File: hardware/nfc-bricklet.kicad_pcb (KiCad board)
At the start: 2 copper layers, 85 x 50 mm, 53 parts, among them J1 CONN_01X03, P1 CON-SENSOR2, U1 XMC130024, U2 PN7150, U3 DRILL, U4 DRILL, U5 DRILL, U6 DRILL, U7 DRILL, U8 DRILL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

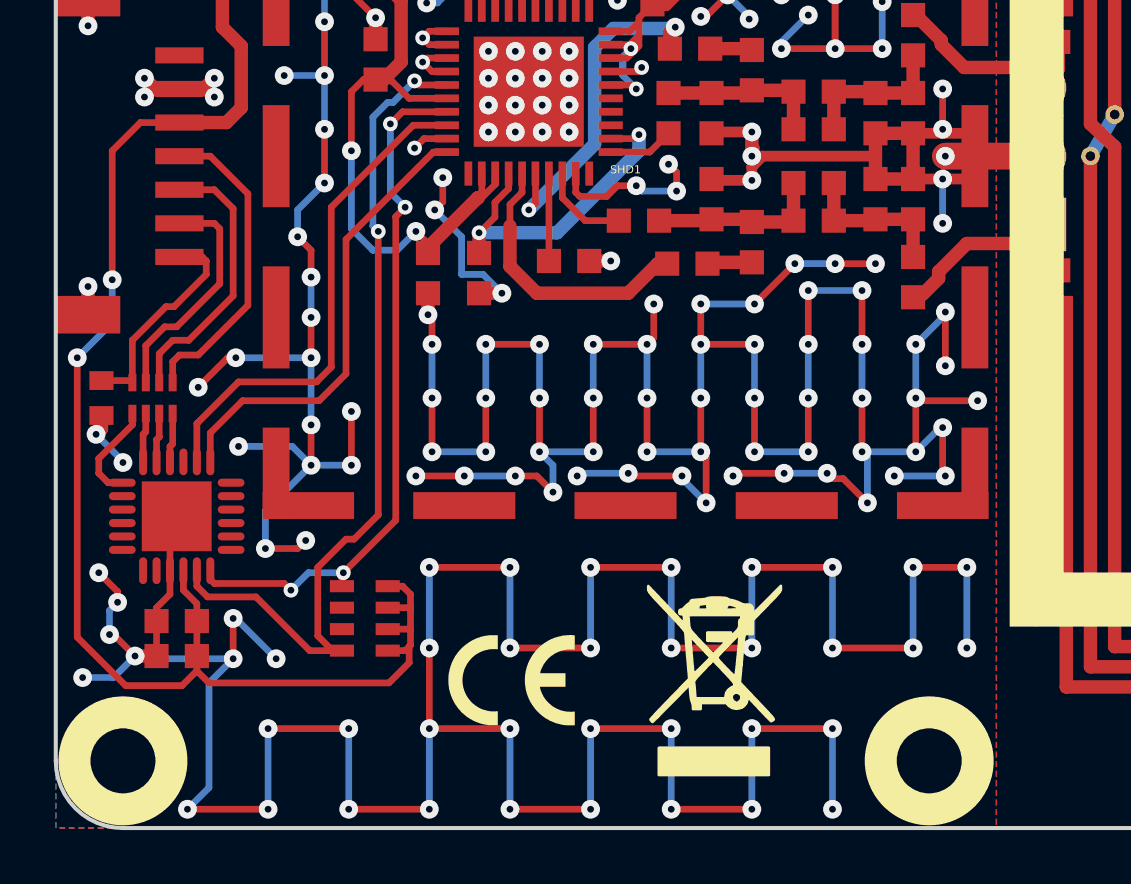
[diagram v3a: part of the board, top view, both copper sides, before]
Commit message: add status led, debug pad, boot pad
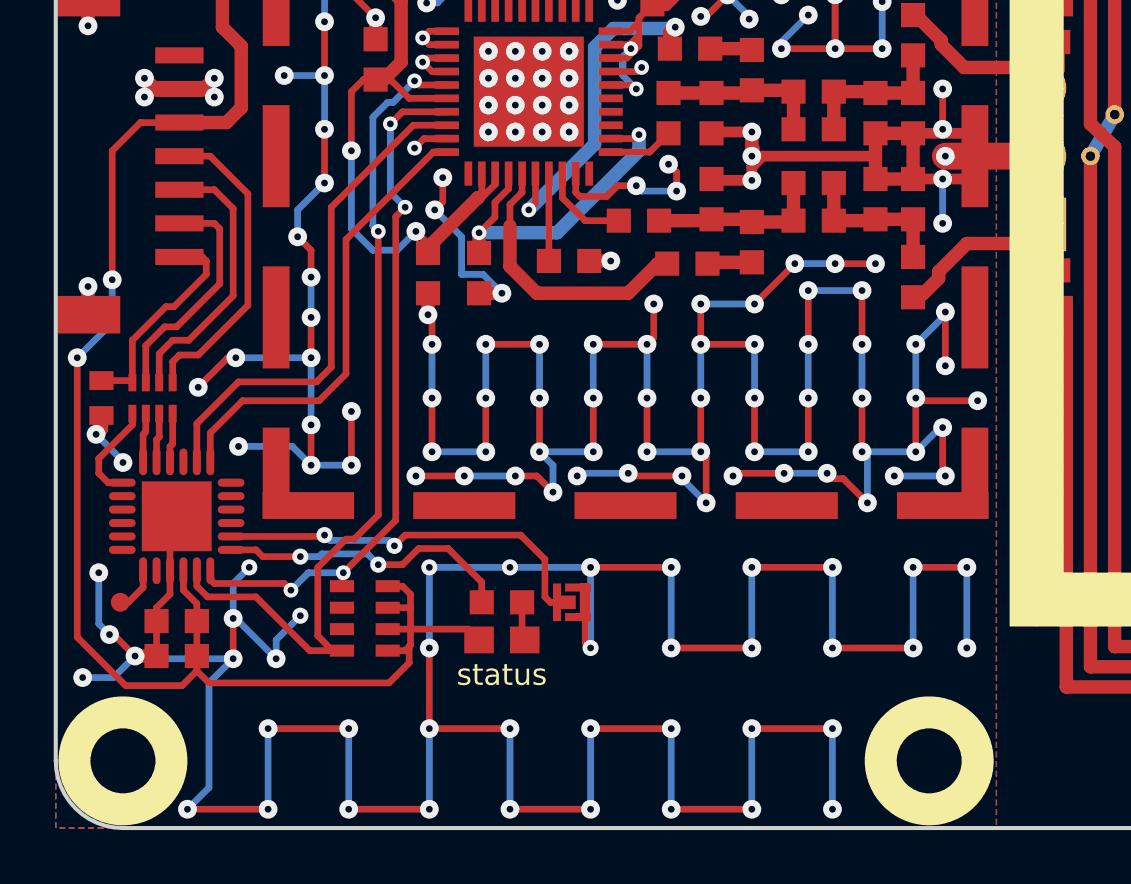
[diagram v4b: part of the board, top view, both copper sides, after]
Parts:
- added D1: blue, D0603E, F.Cu at (127.0, 95.0)
- added P2: BOOT, kicad-libraries:SolderJumper, F.Cu at (129.6, 93.6)
- added P3: DEBUG, kicad-libraries:DEBUG_PAD, F.Cu at (112.8, 93.6)
- added R7: 1k, R0603F, F.Cu at (127.0, 93.6)
- VAL (x2): moved to B.Cu
- moved VAL 20.9 mm to (127.4, 77.0)
- moved VAL 20.7 mm to (120.4, 77.0)
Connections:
- U1 pad 13: (no net) -> Net-(R7-Pad1)
- U1 pad 14: (no net) -> Net-(P2-Pad2)
- U1 pad 7: (no net) -> Net-(P3-Pad1)
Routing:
- net Net-(P2-Pad2): track 0.00 -> 14.7 mm, vias 0 -> 2
- net Net-(R7-Pad1): track 0.00 -> 11.2 mm, vias 0 -> 2
- net VCC: track 114.7 -> 117.4 mm
- net Net-(P3-Pad1): track 0.00 -> 1.70 mm
- net Net-(D1-Pad2): track 0.00 -> 1.44 mm
- net GND: track 611.5 -> 611.6 mm, vias 268 -> 266
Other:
- net class Default: clearance 0.2 -> 0.15
- rule trace_clearance: 0.2 -> 0.15
- board text added: "status"

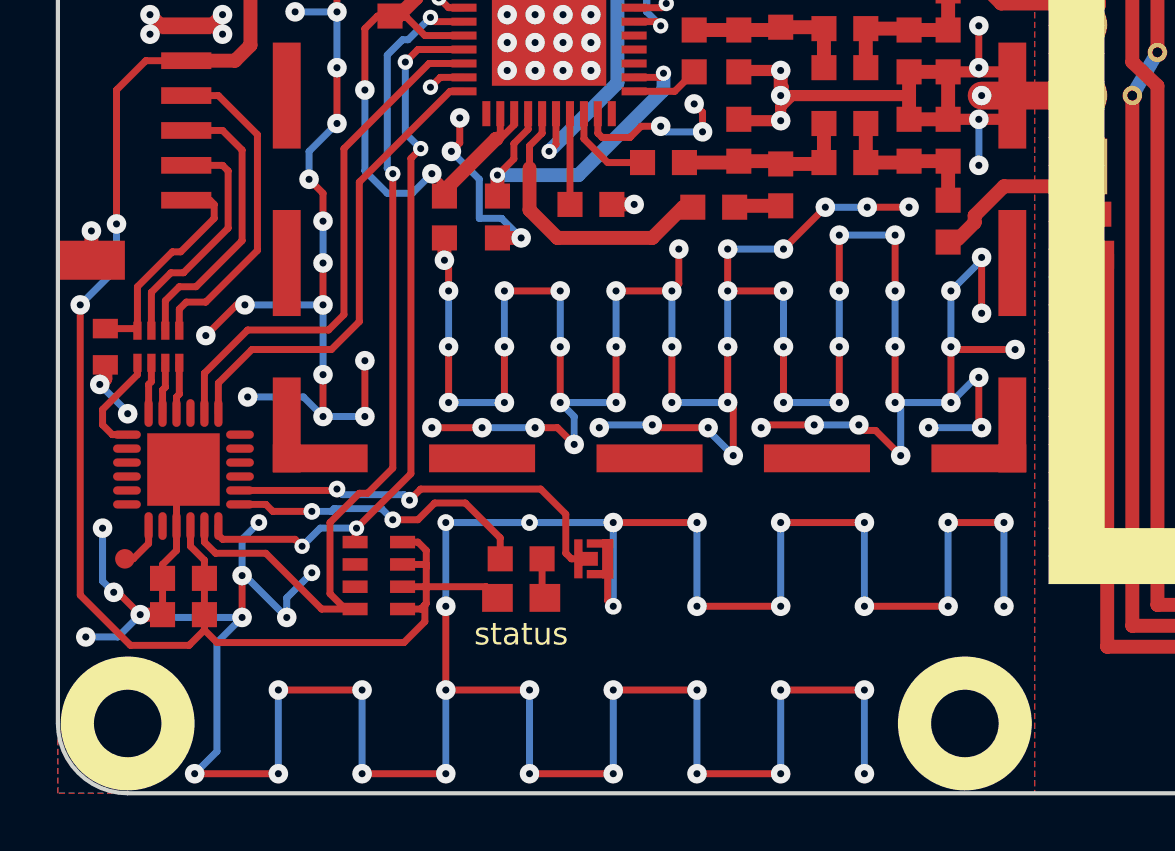
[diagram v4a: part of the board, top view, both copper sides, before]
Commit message: add second led
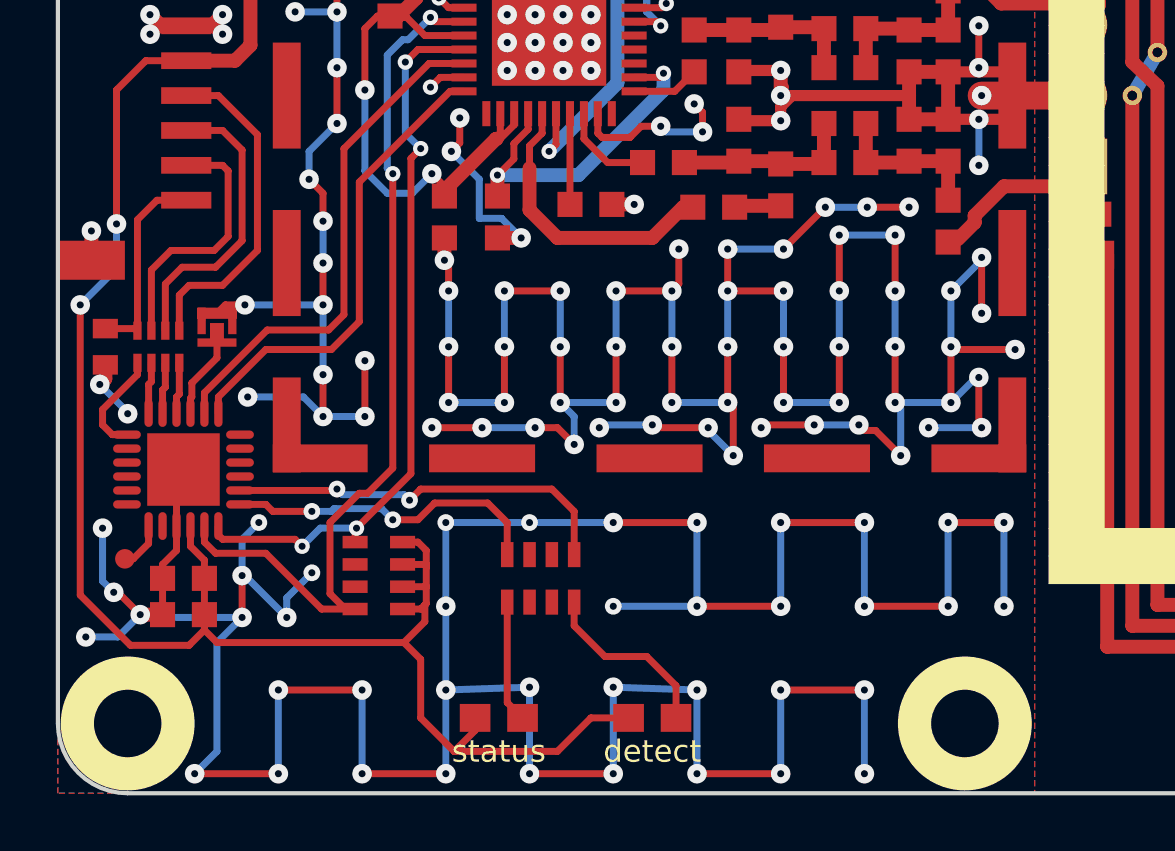
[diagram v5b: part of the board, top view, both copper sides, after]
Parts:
- removed R7: 1k, R0603F
- added D2: green, D0603E, F.Cu at (131.7, 99.3)
- added RP3: 1k, 4X0603, F.Cu at (127.7, 94.3)
- moved P2 15.8 mm to (116.1, 85.3), turned to 270 degrees
- moved D1 4.37 mm to (126.2, 99.3)
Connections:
- U1 pad 14: Net-(P2-Pad2) -> Net-(RP3-Pad4)
- U1 pad 21: (no net) -> Net-(P2-Pad2)
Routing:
- net Net-(RP3-Pad4): track 0.00 -> 14.3 mm, vias 0 -> 2
- net Net-(P2-Pad2): track 14.7 -> 3.32 mm, vias 2 -> 0
- net VCC: track 117.4 -> 127.6 mm
- net Net-(D2-Pad2): track 0.00 -> 6.54 mm
- net GND: track 611.6 -> 608.3 mm, vias 266 -> 265
- net Net-(D1-Pad2): track 1.44 -> 4.38 mm
- net Net-(C1-Pad1): track 8.12 -> 7.26 mm
- net Net-(P1-Pad6): track 8.71 -> 9.35 mm
- net Net-(RP3-Pad1): track 11.2 -> 11.7 mm
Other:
- board text added: "detect"

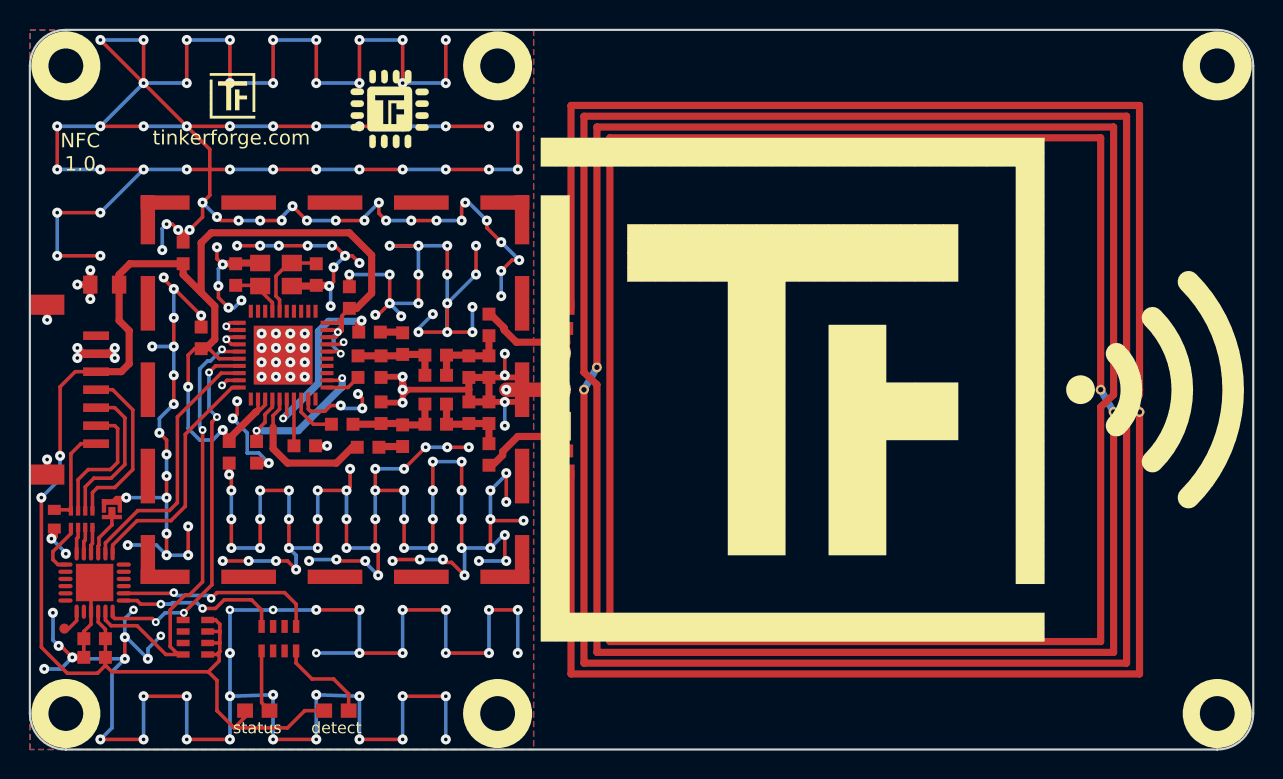
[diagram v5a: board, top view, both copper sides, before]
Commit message: add fiducials, swap sda,scl
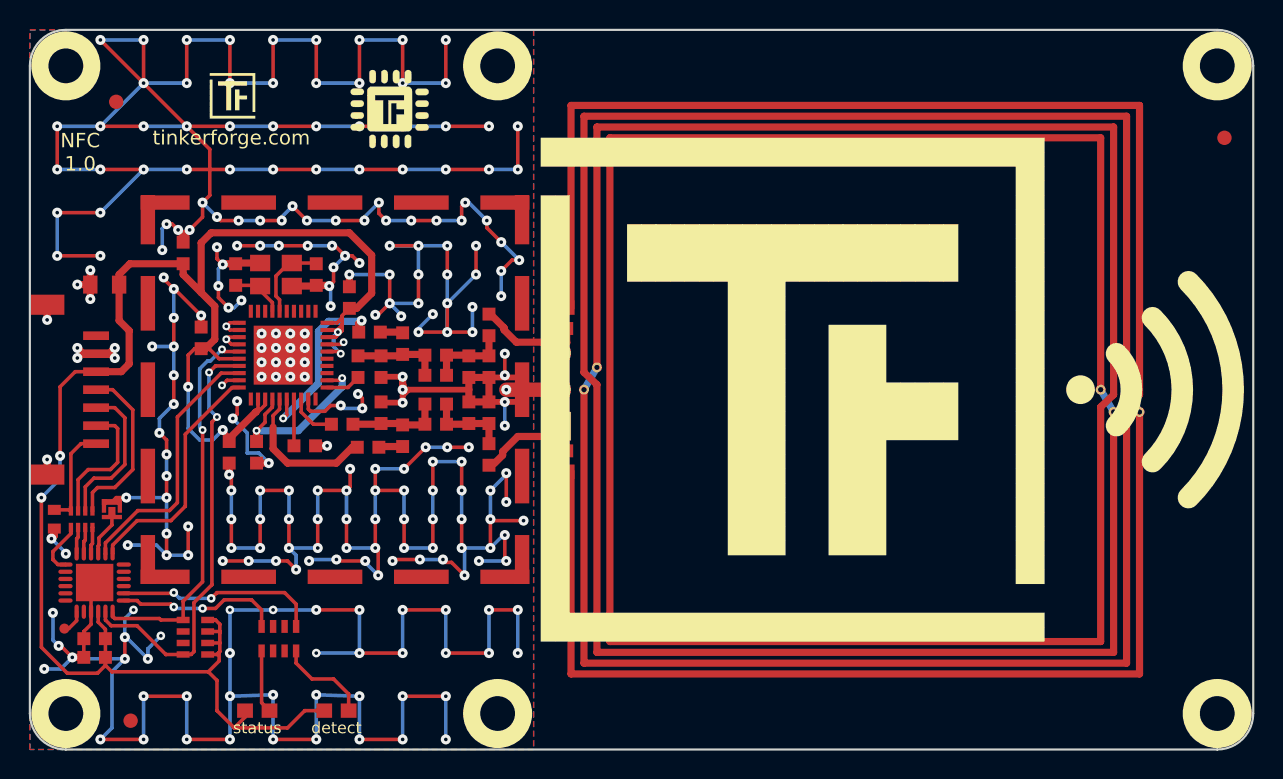
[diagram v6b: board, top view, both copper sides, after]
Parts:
- added Fiducial_Mark: VAL**, kicad-libraries:Fiducial_Mark, F.Cu at (116.4, 57.0)
- added Fiducial_Mark: VAL**, kicad-libraries:Fiducial_Mark, F.Cu at (117.4, 100.0)
- added Fiducial_Mark: VAL**, kicad-libraries:Fiducial_Mark, F.Cu at (193.4, 59.5)
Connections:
- RP2 pad 5: SDA -> SCL
- RP2 pad 8: SCL -> SDA
- U1 pad 11: SDA -> SCL
- U1 pad 12: SCL -> SDA
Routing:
- net SDA: track 32.0 -> 26.8 mm
- net SCL: track 26.6 -> 30.5 mm, vias 4 -> 2

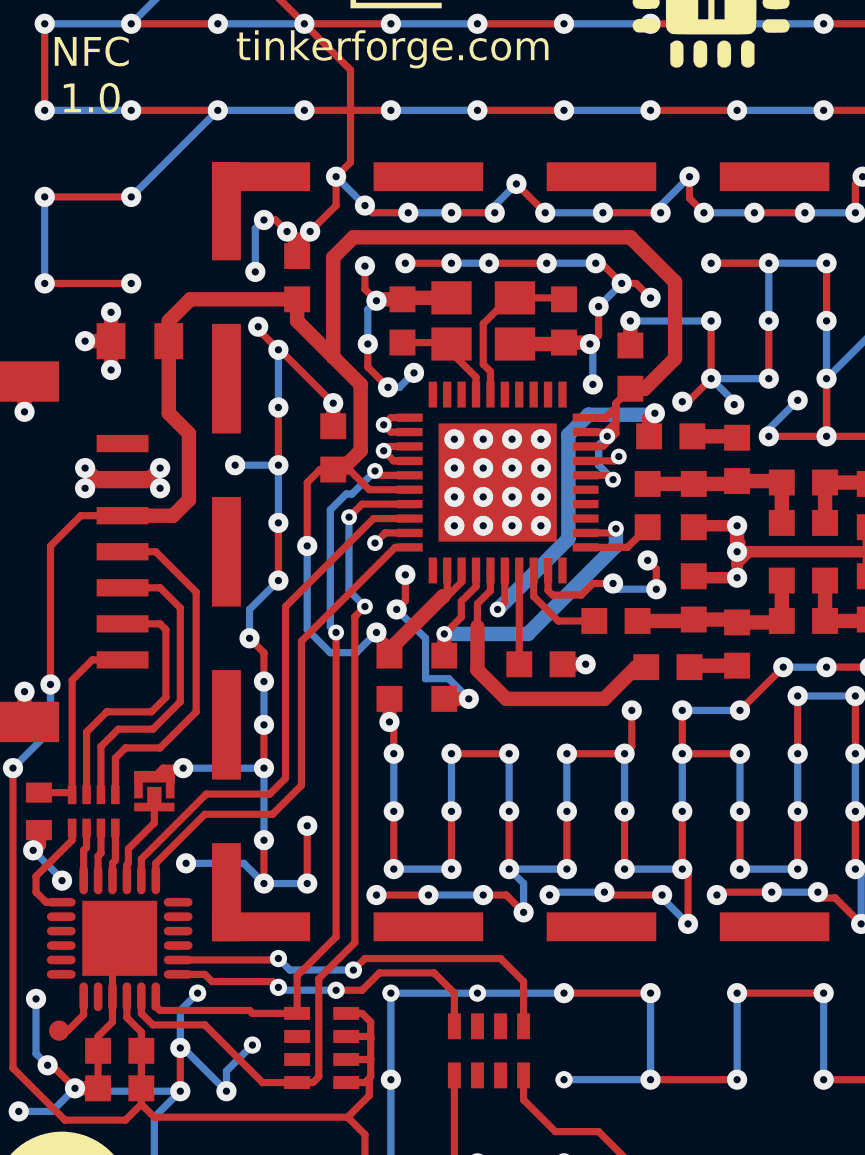
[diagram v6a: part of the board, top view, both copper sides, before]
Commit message: make vdd an island
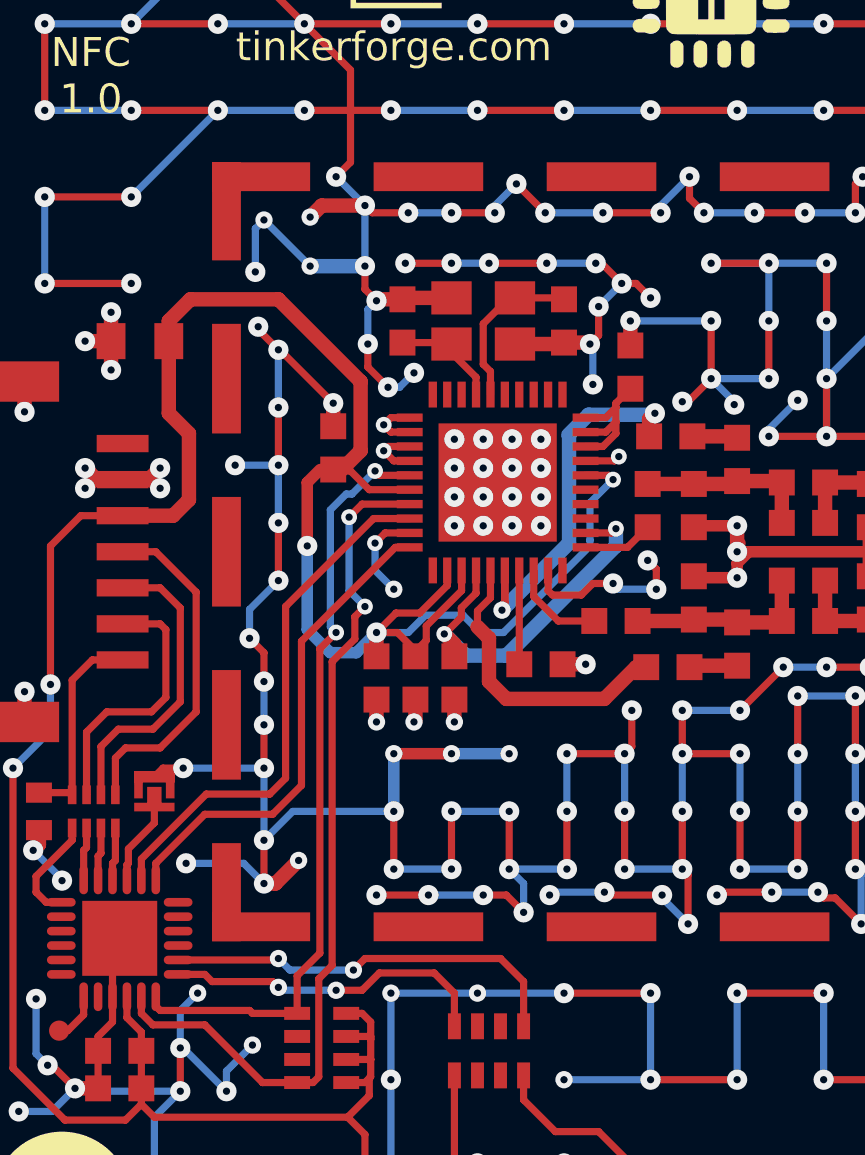
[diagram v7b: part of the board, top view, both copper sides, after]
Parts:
- C10: value 100nF -> 1uF
- moved C9 8.47 mm to (125.2, 81.4), turned to 270 degrees
- moved C8 6.03 mm to (122.3, 73.4)
- moved C7 0.45 mm to (123.8, 81.4)
- moved C12 0.35 mm to (126.5, 81.4)
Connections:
- C10 pad 1: VCC -> Net-(C10-Pad1)
- P1 pad 1: (no net) -> +5V
- U2 pad 28: VCC -> Net-(C10-Pad1)
- U2 pad 29: VCC -> Net-(C10-Pad1)
- U2 pad 30: VCC -> Net-(C10-Pad1)
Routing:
- net VCC: track 127.6 -> 114.2 mm, vias 6 -> 5
- net Net-(C10-Pad1): track 0.00 -> 5.39 mm
- net GND: track 608.3 -> 609.7 mm, vias 265 -> 264
- net Net-(C15-Pad2): track 12.7 -> 14.1 mm
- net Net-(C12-Pad2): track 12.3 -> 13.1 mm
